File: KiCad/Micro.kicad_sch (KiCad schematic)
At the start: 25 parts, among them J1 Conn_01x02, SW1 SW_Push, U1 MCP4725xxx-xCH

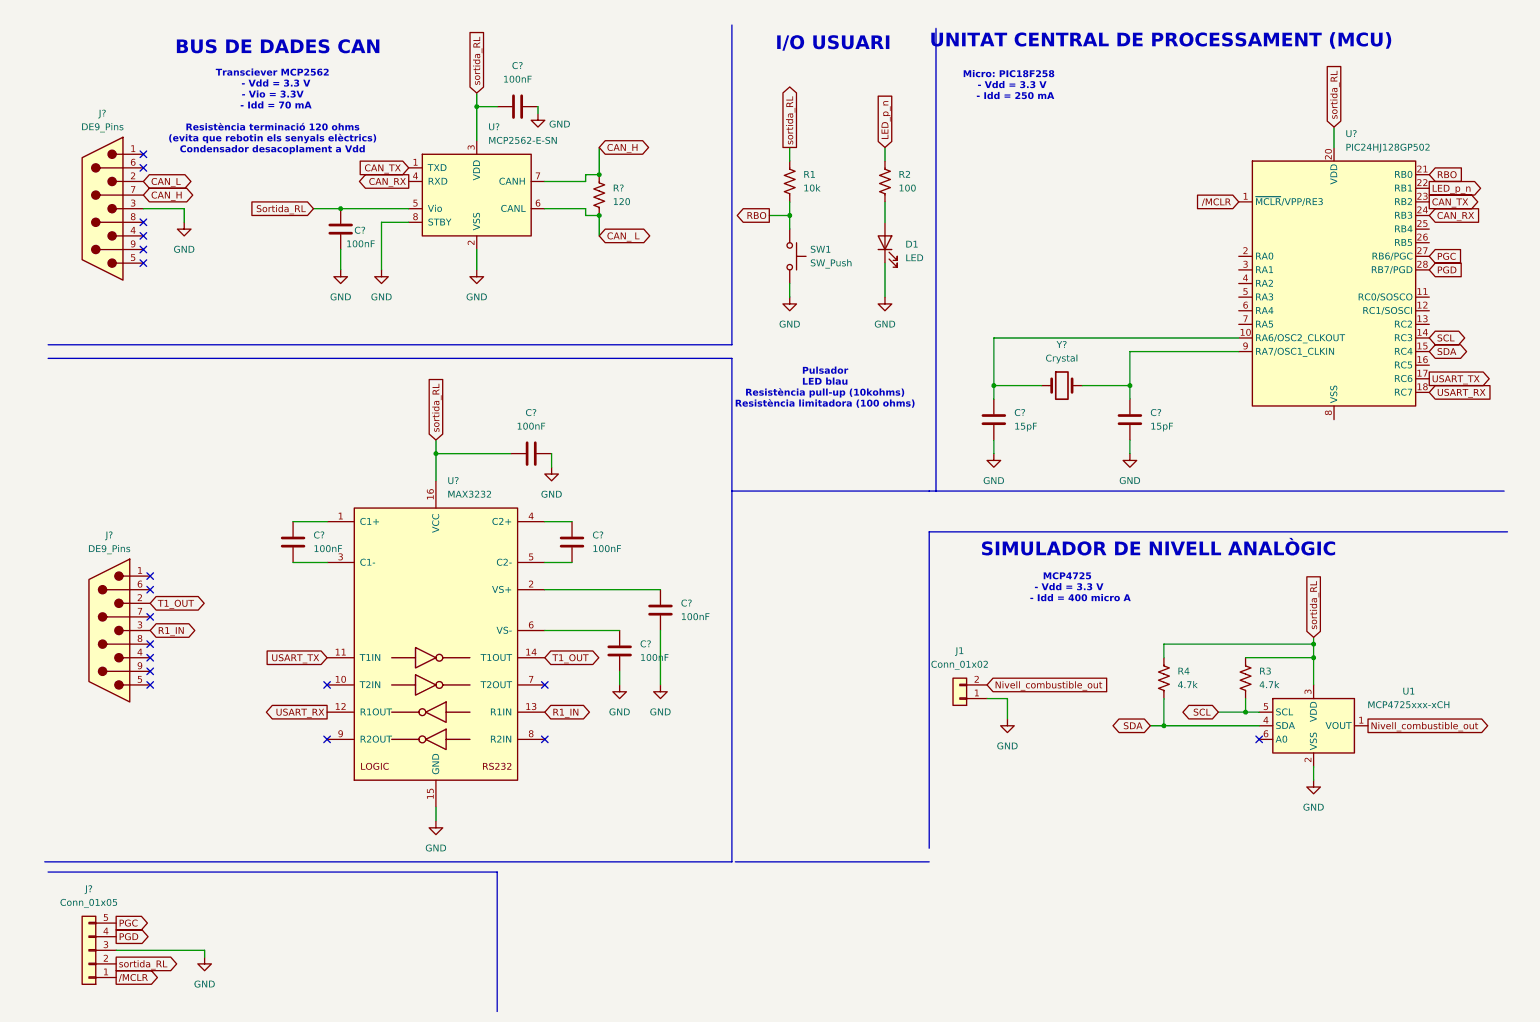
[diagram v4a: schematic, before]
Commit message: millora disseny micro
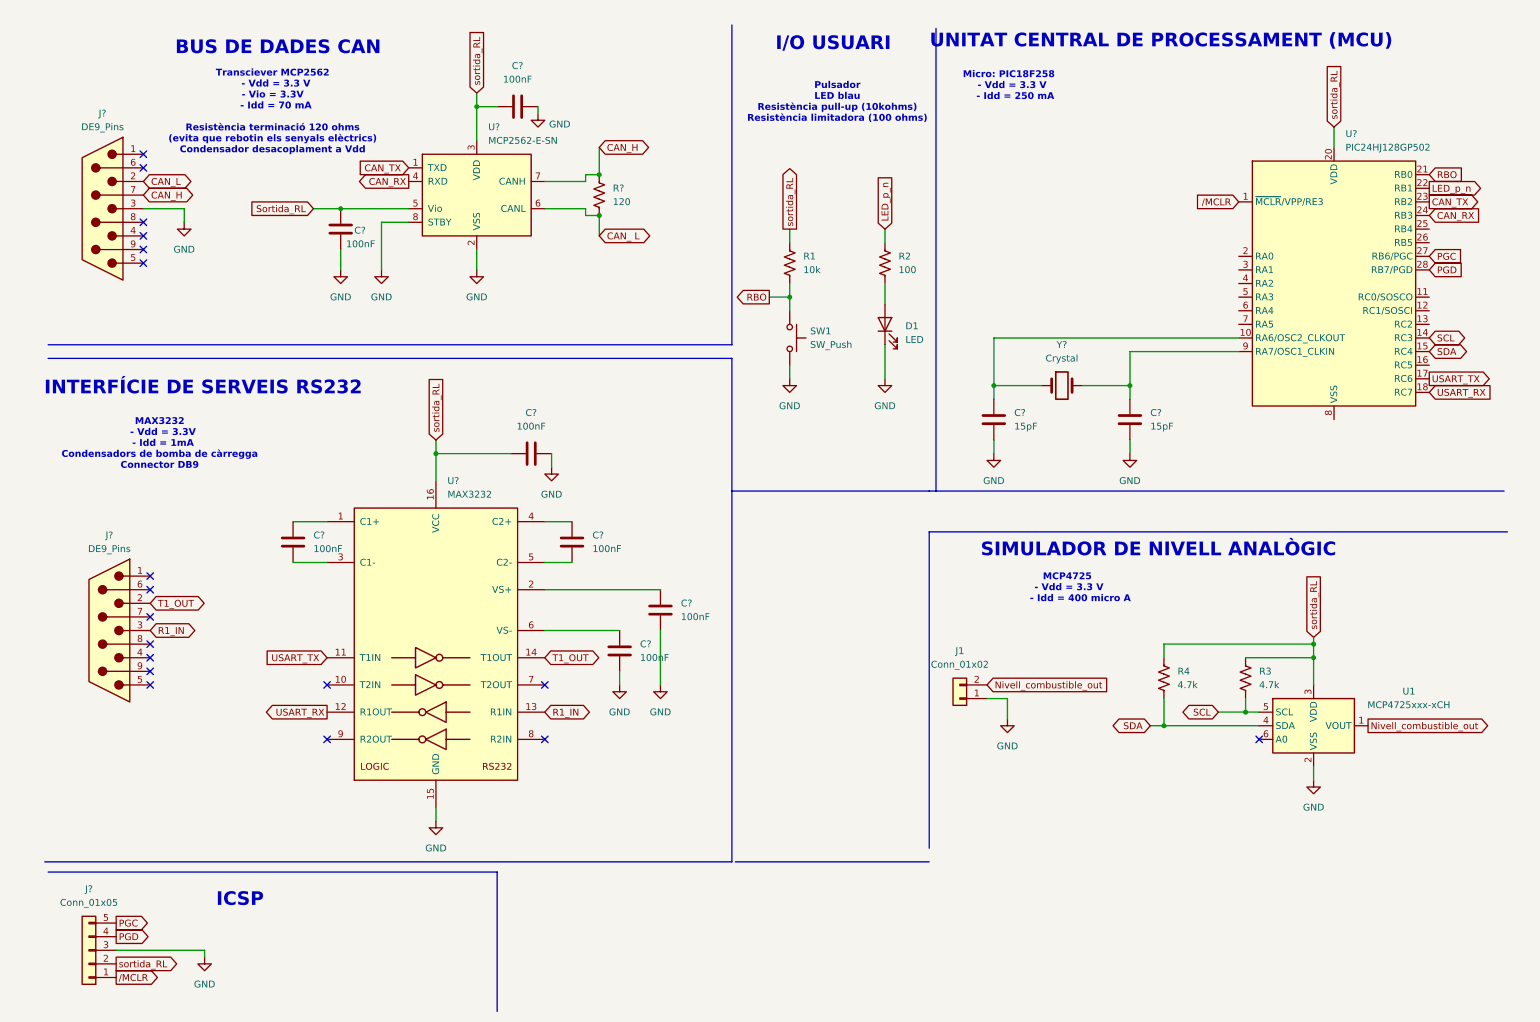
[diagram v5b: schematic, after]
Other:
- note added: "ICSP"
- note added: "INTERFÍCIE DE SERVEIS RS232"
- note added: "MAX3232 - Vdd = 3.3V - Idd = 1mA Condensadors de bomba de càrregga Connector DB9"
- moved on the sheet: D1, R1, R2, SW1
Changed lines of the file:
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@@
 		)
 	)
+	(text "MAX3232\n  - Vdd = 3.3V\n  - Idd = 1mA\nCondensadors de bomba de càrregga\nConnector DB9"
+		(exclude_from_sim no)
+		(at 33.528 90.932 0)
+		(effects
+			(font
+				(size 1.27 1.27)
+				(thickness 0.254)
+				(bold yes)
+			)
+		)
+	)
 	(text "MCP4725\n - Vdd = 3.3 V\n        - Idd = 400 micro A"
 		(exclude_from_sim no)
@@
 		)
 	)
+	(text "ICSP"
+		(exclude_from_sim no)
+		(at 48.514 176.022 0)
+		(effects
+			(font
+				(face "Arial")
+				(size 2.54 2.54)
+				(bold yes)
+				(color 0 0 254 1)
+			)
+		)
+	)
+	(text "INTERFÍCIE DE SERVEIS RS232"
+		(exclude_from_sim no)
+		(at 41.656 80.518 0)
+		(effects
+			(font
+				(face "Arial")
+				(size 2.54 2.54)
+				(thickness 0.254)
+				(bold yes)
+				(color 0 0 254 1)
+			)
+		)
+	)
 	(text "Pulsador\nLED blau\nResistència pull-up (10kohms)\nResistència limitadora (100 ohms)"
 		(exclude_from_sim no)
-		(at 157.734 80.518 0)
+		(at 160.02 27.178 0)
 		(effects
 			(font
@@
 	)
 	(junction
-		(at 151.13 48.26)
+		(at 151.13 63.5)
 		(diameter 0)
 		(color 0 0 0 0)
@@
 	(wire
 		(pts
-			(xy 151.13 60.96) (xy 151.13 63.5)
+			(xy 151.13 76.2) (xy 151.13 78.74)
 		)
 		(stroke
@@
 	(wire
 		(pts
-			(xy 168.91 35.56) (xy 168.91 38.1)
+			(xy 168.91 50.8) (xy 168.91 53.34)
 		)
 		(stroke
@@
 	(wire
 		(pts
-			(xy 168.91 45.72) (xy 168.91 49.53)
+			(xy 168.91 60.96) (xy 168.91 64.77)
 		)
 		(stroke
@@
 	(wire
 		(pts
-			(xy 151.13 45.72) (xy 151.13 48.26)
+			(xy 151.13 60.96) (xy 151.13 63.5)
 		)
 		(stroke
@@
 	(wire
 		(pts
-			(xy 147.32 48.26) (xy 151.13 48.26)
+			(xy 147.32 63.5) (xy 151.13 63.5)
 		)
 		(stroke
@@
 	(wire
 		(pts
-			(xy 151.13 48.26) (xy 151.13 50.8)
+			(xy 151.13 63.5) (xy 151.13 66.04)
 		)
 		(stroke
@@
 	(wire
 		(pts
-			(xy 151.13 35.56) (xy 151.13 38.1)
+			(xy 151.13 50.8) (xy 151.13 53.34)
 		)
 		(stroke
@@
 	(wire
 		(pts
-			(xy 168.91 57.15) (xy 168.91 63.5)
+			(xy 168.91 72.39) (xy 168.91 78.74)
 		)
 		(stroke
@@
 	(global_label "LED_p_n"
 		(shape input)
-		(at 168.91 35.56 90)
+		(at 168.91 50.8 90)
 		(fields_autoplaced yes)
 		(effects
@@
 		)
 		(property "Intersheetrefs" "${INTERSHEET_REFS}"
-			(at 168.91 24.8945 90)
+			(at 168.91 40.1345 90)
 			(effects
 				(font
@@
 	(global_label "sortida_RL"
 		(shape output)
-		(at 151.13 35.56 90)
+		(at 151.13 50.8 90)
 		(fields_autoplaced yes)
 		(effects
@@
 		)
 		(property "Intersheetrefs" "${INTERSHEET_REFS}"
-			(at 151.13 22.7173 90)
+			(at 151.13 37.9573 90)
 			(effects
 				(font
@@
 	(global_label "RBO"
 		(shape output)
-		(at 147.32 48.26 180)
+		(at 147.32 63.5 180)
 		(fields_autoplaced yes)
 		(effects
@@
 		)
 		(property "Intersheetrefs" "${INTERSHEET_REFS}"
-			(at 140.4643 48.26 0)
+			(at 140.4643 63.5 0)
 			(effects
 				(font
@@
 	(symbol
 		(lib_id "Device:R_US")
-		(at 168.91 41.91 0)
+		(at 168.91 57.15 0)
 		(unit 1)
 		(exclude_from_sim no)
@@
 		(fields_autoplaced yes)
 		(property "Reference" "R2"
-			(at 171.45 40.6399 0)
+			(at 171.45 55.8799 0)
 			(effects
 				(font
@@
 		)
 		(property "Value" "100"
-			(at 171.45 43.1799 0)
+			(at 171.45 58.4199 0)
 			(effects
 				(font
@@
 		)
 		(property "Footprint" ""
-			(at 169.926 42.164 90)
+			(at 169.926 57.404 90)
 			(effects
 				(font
@@
 		)
 		(property "Datasheet" "~"
-			(at 168.91 41.91 0)
+			(at 168.91 57.15 0)
 			(effects
 				(font
@@
 		)
 		(property "Description" "Resistor, US symbol"
-			(at 168.91 41.91 0)
+			(at 168.91 57.15 0)
 			(effects
 				(font
@@
 	(symbol
 		(lib_id "Switch:SW_Push")
-		(at 151.13 55.88 270)
+		(at 151.13 71.12 270)
 		(unit 1)
 		(exclude_from_sim no)
@@
 		(fields_autoplaced yes)
 		(property "Reference" "SW1"
-			(at 154.94 54.6099 90)
+			(at 154.94 69.8499 90)
 			(effects
 				(font
@@
 		)
 		(property "Value" "SW_Push"
-			(at 154.94 57.1499 90)
+			(at 154.94 72.3899 90)
 			(effects
 				(font
@@
 		)
 		(property "Footprint" ""
-			(at 156.21 55.88 0)
+			(at 156.21 71.12 0)
 			(effects
 				(font
@@
 		)
 		(property "Datasheet" "~"
-			(at 156.21 55.88 0)
+			(at 156.21 71.12 0)
 			(effects
 				(font
@@
 		)
 		(property "Description" "Push button switch, generic, two pins"
-			(at 151.13 55.88 0)
+			(at 151.13 71.12 0)
 			(effects
 				(font
@@
 	(symbol
 		(lib_id "Device:LED")
-		(at 168.91 53.34 90)
+		(at 168.91 68.58 90)
 		(unit 1)
 		(exclude_from_sim no)
@@
 		(fields_autoplaced yes)
 		(property "Reference" "D1"
-			(at 172.72 53.6574 90)
+			(at 172.72 68.8974 90)
 			(effects
 				(font
@@
 		)
 		(property "Value" "LED"
-			(at 172.72 56.1974 90)
+			(at 172.72 71.4374 90)
 			(effects
 				(font
@@
 		)
 		(property "Footprint" ""
-			(at 168.91 53.34 0)
+			(at 168.91 68.58 0)
 			(effects
 				(font
@@
 		)
 		(property "Datasheet" "~"
-			(at 168.91 53.34 0)
+			(at 168.91 68.58 0)
 			(effects
 				(font
@@
 		)
 		(property "Description" "Light emitting diode"
-			(at 168.91 53.34 0)
+			(at 168.91 68.58 0)
 			(effects
 				(font
@@
 		)
 		(property "Sim.Pins" "1=K 2=A"
-			(at 168.91 53.34 0)
+			(at 168.91 68.58 0)
 			(effects
 				(font
@@
 	(symbol
 		(lib_id "Device:R_US")
-		(at 151.13 41.91 0)
+		(at 151.13 57.15 0)
 		(unit 1)
 		(exclude_from_sim no)
@@
 		(fields_autoplaced yes)
 		(property "Reference" "R1"
-			(at 153.67 40.6399 0)
+			(at 153.67 55.8799 0)
 			(effects
 				(font
@@
 		)
 		(property "Value" "10k"
-			(at 153.67 43.1799 0)
+			(at 153.67 58.4199 0)
 			(effects
 				(font
@@
 		)
 		(property "Footprint" ""
-			(at 152.146 42.164 90)
+			(at 152.146 57.404 90)
 			(effects
 				(font
@@
 		)
 		(property "Datasheet" "~"
-			(at 151.13 41.91 0)
+			(at 151.13 57.15 0)
 			(effects
 				(font
@@
 		)
 		(property "Description" "Resistor, US symbol"
-			(at 151.13 41.91 0)
+			(at 151.13 57.15 0)
 			(effects
 				(font
@@
 	(symbol
 		(lib_id "power:GND")
-		(at 151.13 63.5 0)
+		(at 151.13 78.74 0)
 		(unit 1)
 		(exclude_from_sim no)
@@
 		(fields_autoplaced yes)
 		(property "Reference" "#PWR01"
-			(at 151.13 69.85 0)
+			(at 151.13 85.09 0)
 			(effects
 				(font
@@
 		)
 		(property "Value" "GND"
-			(at 151.13 68.58 0)
+			(at 151.13 83.82 0)
 			(effects
 				(font
@@
 		)
 		(property "Footprint" ""
-			(at 151.13 63.5 0)
+			(at 151.13 78.74 0)
 			(effects
 				(font
@@
 		)
 		(property "Datasheet" ""
-			(at 151.13 63.5 0)
+			(at 151.13 78.74 0)
 			(effects
 				(font
@@
 		)
 		(property "Description" "Power symbol creates a global label with name \"GND\" , ground"
-			(at 151.13 63.5 0)
+			(at 151.13 78.74 0)
 			(effects
 				(font
@@
 	(symbol
 		(lib_id "power:GND")
-		(at 168.91 63.5 0)
+		(at 168.91 78.74 0)
 		(unit 1)
 		(exclude_from_sim no)
@@
 		(fields_autoplaced yes)
 		(property "Reference" "#PWR02"
-			(at 168.91 69.85 0)
+			(at 168.91 85.09 0)
 			(effects
 				(font
@@
 		)
 		(property "Value" "GND"
-			(at 168.91 68.58 0)
+			(at 168.91 83.82 0)
 			(effects
 				(font
@@
 		)
 		(property "Footprint" ""
-			(at 168.91 63.5 0)
+			(at 168.91 78.74 0)
 			(effects
 				(font
@@
 		)
 		(property "Datasheet" ""
-			(at 168.91 63.5 0)
+			(at 168.91 78.74 0)
 			(effects
 				(font
@@
 		)
 		(property "Description" "Power symbol creates a global label with name \"GND\" , ground"
-			(at 168.91 63.5 0)
+			(at 168.91 78.74 0)
 			(effects
 				(font

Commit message: Part de potencia acabada, concretar certs pins del micro
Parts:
- gave numbers to parts that had none: 17
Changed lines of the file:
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@@
 		(dnp no)
 		(fields_autoplaced yes)
-		(property "Reference" "C?"
+		(property "Reference" "C5"
 			(at 62.23 107.9499 0)
 			(effects
@@
 		(dnp no)
 		(fields_autoplaced yes)
-		(property "Reference" "#PWR?"
+		(property "Reference" "#PWR08"
 			(at 41.91 193.04 0)
 			(effects
@@
 		(dnp no)
 		(fields_autoplaced yes)
-		(property "Reference" "R2"
+		(property "Reference" "R?"
 			(at 171.45 55.8799 0)
 			(effects
@@
 				)
 			)
+			(project "Combustible_projecte"
+				(path "/c989196d-f442-462e-ad13-2ff17993bc1b/73a8a135-7ac0-4af3-83b0-52460225a0ec"
+					(reference "R?")
+					(unit 1)
+				)
+			)
 		)
 	)
@@
 		(dnp no)
 		(fields_autoplaced yes)
-		(property "Reference" "#PWR?"
+		(property "Reference" "#PWR012"
 			(at 106.68 101.6 0)
 			(effects
@@
 		(dnp no)
 		(fields_autoplaced yes)
-		(property "Reference" "#PWR?"
+		(property "Reference" "#PWR09"
 			(at 85.09 167.64 0)
 			(effects
@@
 		(dnp no)
 		(fields_autoplaced yes)
-		(property "Reference" "C?"
+		(property "Reference" "C1"
 			(at 100.33 20.32 90)
 			(effects
@@
 		(dnp no)
 		(fields_autoplaced yes)
-		(property "Reference" "#PWR?"
+		(property "Reference" "#PWR07"
 			(at 189.23 99.06 0)
 			(effects
@@
 		(dnp no)
 		(fields_autoplaced yes)
-		(property "Reference" "C?"
+		(property "Reference" "C7"
 			(at 130.81 120.6499 0)
 			(effects
@@
 		(dnp no)
 		(fields_autoplaced yes)
-		(property "Reference" "#PWR03"
+		(property "Reference" "#PWR?"
 			(at 248.92 160.02 0)
 			(effects
@@
 				)
 			)
+			(project "Combustible_projecte"
+				(path "/c989196d-f442-462e-ad13-2ff17993bc1b/73a8a135-7ac0-4af3-83b0-52460225a0ec"
+					(reference "#PWR?")
+					(unit 1)
+				)
+			)
 		)
 	)
@@
 		(on_board yes)
 		(dnp no)
-		(property "Reference" "#PWR?"
+		(property "Reference" "#PWR06"
 			(at 214.63 99.06 0)
 			(effects
@@
 		(on_board yes)
 		(dnp no)
-		(property "Reference" "J1"
+		(property "Reference" "J?"
 			(at 182.88 129.54 0)
 			(effects
@@
 				)
 			)
+			(project "Combustible_projecte"
+				(path "/c989196d-f442-462e-ad13-2ff17993bc1b/73a8a135-7ac0-4af3-83b0-52460225a0ec"
+					(reference "J?")
+					(unit 1)
+				)
+			)
 		)
 	)
@@
 		(dnp no)
 		(fields_autoplaced yes)
-		(property "Reference" "#PWR?"
+		(property "Reference" "#PWR02"
 			(at 38.1 55.88 0)
 			(effects
@@
 		(on_board yes)
 		(dnp no)
-		(property "Reference" "#PWR?"
+		(property "Reference" "#PWR04"
 			(at 104.14 35.56 0)
 			(effects
@@
 		(dnp no)
 		(fields_autoplaced yes)
-		(property "Reference" "#PWR?"
+		(property "Reference" "#PWR010"
 			(at 119.38 142.24 0)
 			(effects
@@
 		(dnp no)
 		(fields_autoplaced yes)
-		(property "Reference" "U?"
+		(property "Reference" "U1"
 			(at 254.8733 33.02 0)
 			(effects
@@
 		(dnp no)
 		(fields_autoplaced yes)
-		(property "Reference" "SW1"
+		(property "Reference" "SW?"
 			(at 154.94 69.8499 90)
 			(effects
@@
 				)
 			)
+			(project "Combustible_projecte"
+				(path "/c989196d-f442-462e-ad13-2ff17993bc1b/73a8a135-7ac0-4af3-83b0-52460225a0ec"
+					(reference "SW?")
+					(unit 1)
+				)
+			)
 		)
 	)
@@
 		(dnp no)
 		(fields_autoplaced yes)
-		(property "Reference" "D1"
+		(property "Reference" "D?"
 			(at 172.72 68.8974 90)
 			(effects
@@
 				)
 			)
+			(project "Combustible_projecte"
+				(path "/c989196d-f442-462e-ad13-2ff17993bc1b/73a8a135-7ac0-4af3-83b0-52460225a0ec"
+					(reference "D?")
+					(unit 1)
+				)
+			)
 		)
 	)
@@
 		(dnp no)
 		(fields_autoplaced yes)
-		(property "Reference" "R3"
+		(property "Reference" "R?"
 			(at 238.76 133.3499 0)
 			(effects
@@
 				)
 			)
+			(project "Combustible_projecte"
+				(path "/c989196d-f442-462e-ad13-2ff17993bc1b/73a8a135-7ac0-4af3-83b0-52460225a0ec"
+					(reference "R?")
+					(unit 1)
+				)
+			)
 		)
 	)
@@
 		(dnp no)
 		(fields_autoplaced yes)
-		(property "Reference" "R1"
+		(property "Reference" "R?"
 			(at 153.67 55.8799 0)
 			(effects
@@
 				)
 			)
+			(project "Combustible_projecte"
+				(path "/c989196d-f442-462e-ad13-2ff17993bc1b/73a8a135-7ac0-4af3-83b0-52460225a0ec"
+					(reference "R?")
+					(unit 1)
+				)
+			)
 		)
 	)
@@
 		(dnp no)
 		(fields_autoplaced yes)
-		(property "Reference" "#PWR?"
+		(property "Reference" "#PWR05"
 			(at 67.31 64.77 0)
 			(effects
@@
 		(dnp no)
 		(fields_autoplaced yes)
-		(property "Reference" "#PWR?"
+		(property "Reference" "#PWR03"
 			(at 92.71 64.77 0)
 			(effects
@@
 		(dnp no)
 		(fields_autoplaced yes)
-		(property "Reference" "J?"
+		(property "Reference" "J1"
 			(at 22.86 29.21 0)
 			(effects
@@
 		(dnp no)
 		(fields_autoplaced yes)
-		(property "Reference" "C?"
+		(property "Reference" "C8"
 			(at 123.19 128.2699 0)
 			(effects
@@
 		(dnp no)
 		(fields_autoplaced yes)
-		(property "Reference" "C?"
+		(property "Reference" "C9"
 			(at 102.87 85.09 90)
 			(effects
@@
 		(dnp no)
 		(fields_autoplaced yes)
-		(property "Reference" "#PWR04"
+		(property "Reference" "#PWR?"
 			(at 191.77 148.59 0)
 			(effects
@@
 				)
 			)
+			(project "Combustible_projecte"
+				(path "/c989196d-f442-462e-ad13-2ff17993bc1b/73a8a135-7ac0-4af3-83b0-52460225a0ec"
+					(reference "#PWR?")
+					(unit 1)
+				)
+			)
 		)
 	)
@@
 		(dnp no)
 		(fields_autoplaced yes)
-		(property "Reference" "U1"
+		(property "Reference" "U?"
 			(at 266.7 137.0898 0)
 			(effects
@@
 				)
 			)
+			(project "Combustible_projecte"
+				(path "/c989196d-f442-462e-ad13-2ff17993bc1b/73a8a135-7ac0-4af3-83b0-52460225a0ec"
+					(reference "U?")
+					(unit 1)
+				)
+			)
 		)
 	)
@@
 		(dnp no)
 		(fields_autoplaced yes)
-		(property "Reference" "#PWR01"
+		(property "Reference" "#PWR?"
 			(at 151.13 85.09 0)
 			(effects
@@
 				)
 			)
+			(project "Combustible_projecte"
+				(path "/c989196d-f442-462e-ad13-2ff17993bc1b/73a8a135-7ac0-4af3-83b0-52460225a0ec"
+					(reference "#PWR?")
+					(unit 1)
+				)
+			)
 		)
 	)
@@
 		(dnp no)
 		(fields_autoplaced yes)
-		(property "Reference" "J?"
+		(property "Reference" "J2"
 			(at 24.13 107.95 0)
 			(effects
@@
 		(on_board yes)
 		(dnp no)
-		(property "Reference" "C?"
+		(property "Reference" "C2"
 			(at 69.85 51.054 0)
 			(effects
@@
 		(dnp no)
 		(fields_autoplaced yes)
-		(property "Reference" "#PWR02"
+		(property "Reference" "#PWR?"
 			(at 168.91 85.09 0)
 			(effects
@@
 				)
 			)
+			(project "Combustible_projecte"
+				(path "/c989196d-f442-462e-ad13-2ff17993bc1b/73a8a135-7ac0-4af3-83b0-52460225a0ec"
+					(reference "#PWR?")
+					(unit 1)
+				)
+			)
 		)
 	)
@@
 		(dnp no)
 		(fields_autoplaced yes)
-		(property "Reference" "R4"
+		(property "Reference" "R?"
 			(at 223.52 133.3499 0)
 			(effects
@@
 				)
 			)
+			(project "Combustible_projecte"
+				(path "/c989196d-f442-462e-ad13-2ff17993bc1b/73a8a135-7ac0-4af3-83b0-52460225a0ec"
+					(reference "R?")
+					(unit 1)
+				)
+			)
 		)
 	)
@@
 		(dnp no)
 		(fields_autoplaced yes)
-		(property "Reference" "C?"
+		(property "Reference" "C6"
 			(at 114.3 107.9499 0)
 			(effects
@@
 		(dnp no)
 		(fields_autoplaced yes)
-		(property "Reference" "#PWR?"
+		(property "Reference" "#PWR011"
 			(at 127 142.24 0)
 			(effects
@@
 		(dnp no)
 		(fields_autoplaced yes)
-		(property "Reference" "U?"
+		(property "Reference" "U2"
 			(at 94.8533 31.75 0)
 			(effects
@@
 		(dnp no)
 		(fields_autoplaced yes)
-		(property "Reference" "C?"
+		(property "Reference" "C4"
 			(at 193.04 85.0899 0)
 			(effects
@@
 		(dnp no)
 		(fields_autoplaced yes)
-		(property "Reference" "Y?"
+		(property "Reference" "Y1"
 			(at 201.93 72.39 0)
 			(effects
@@
 		(dnp no)
 		(fields_autoplaced yes)
-		(property "Reference" "C?"
+		(property "Reference" "C3"
 			(at 218.44 85.0899 0)
 			(effects
@@
 		(dnp no)
 		(fields_autoplaced yes)
-		(property "Reference" "R?"
+		(property "Reference" "R1"
 			(at 118.11 43.1799 0)
 			(effects
@@
 		(dnp no)
 		(fields_autoplaced yes)
-		(property "Reference" "#PWR?"
+		(property "Reference" "#PWR01"
 			(at 74.93 64.77 0)
 			(effects
@@
 		(dnp no)
 		(fields_autoplaced yes)
-		(property "Reference" "U?"
+		(property "Reference" "U3"
 			(at 87.2333 97.79 0)
 			(effects
@@
 		(dnp no)
 		(fields_autoplaced yes)
-		(property "Reference" "J?"
+		(property "Reference" "J3"
 			(at 20.32 173.99 0)
 			(effects
